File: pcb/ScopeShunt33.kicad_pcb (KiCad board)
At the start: 2 copper layers, 50 x 50 mm, 35 parts, among them J1 Screw_Terminal_01x02, J2 Conn_Coaxial

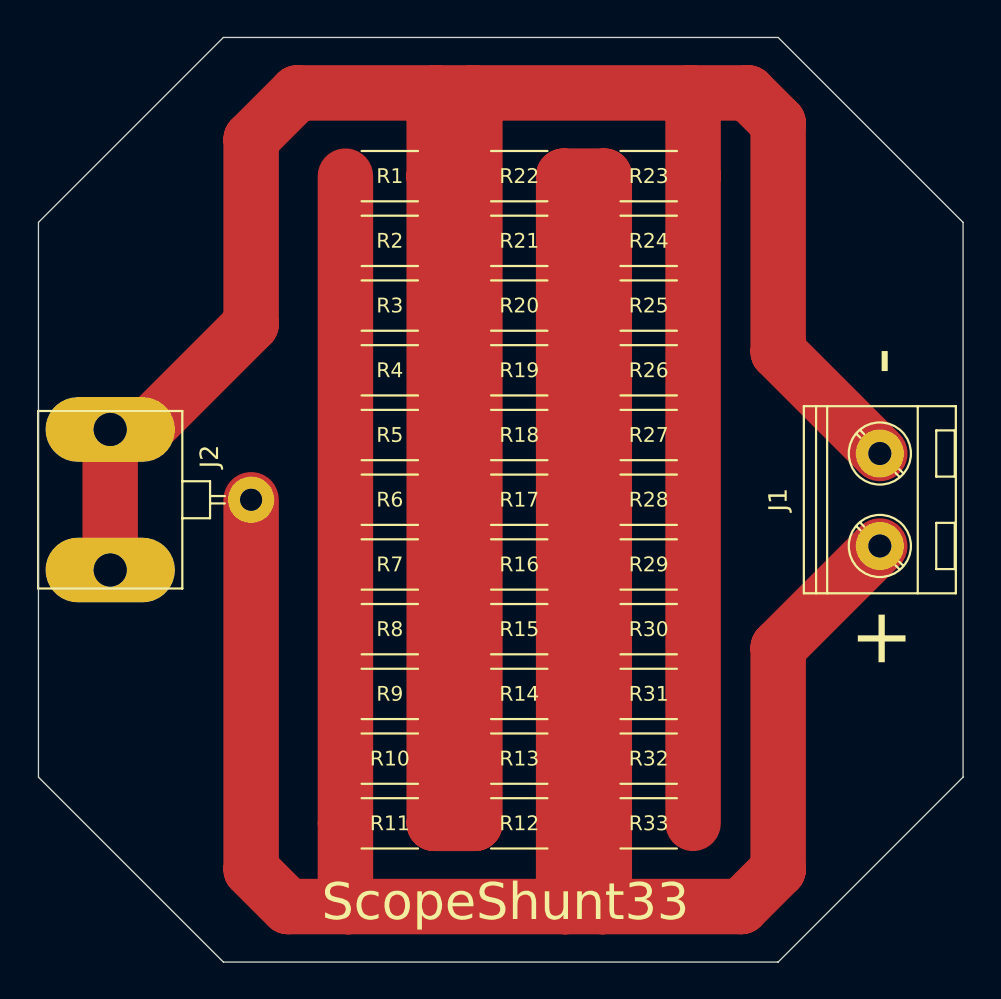
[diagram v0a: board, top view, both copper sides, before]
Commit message: smaller pcb
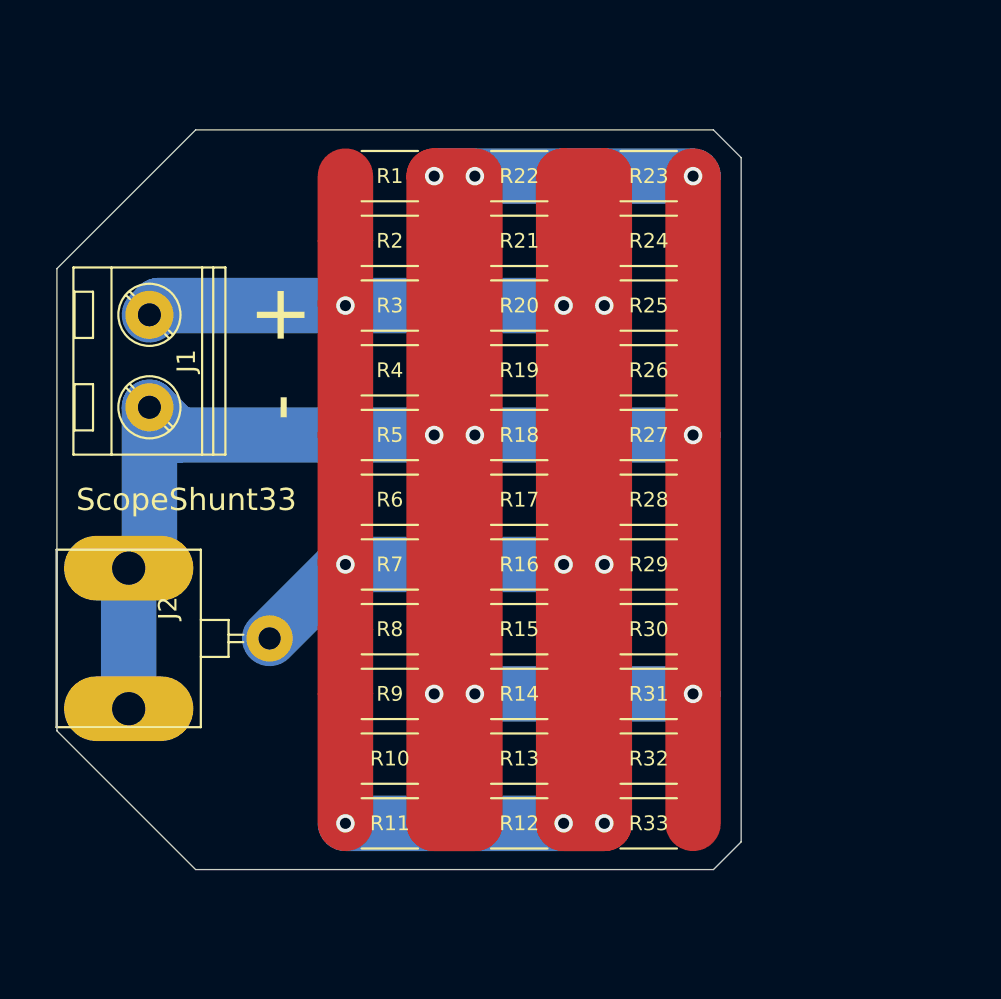
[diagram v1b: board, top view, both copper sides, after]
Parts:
- moved J1 39.6 mm to (131.0, 95.0), turned to 90 degrees
- moved J2 7.57 mm to (137.5, 107.5)
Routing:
- net /+: track 193.0 -> 168.0 mm, vias 0 -> 9
- net /-: track 201.0 -> 184.0 mm, vias 0 -> 9
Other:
- board size 50 x 50 mm -> 37 x 40 mm
- board text added: "Connect + & - in series with load"
- board text added: "LOAD"
- board text added: "SCOPE"
- board text added: "for measuring current with oscilloscope"
- board text added: "github.com/bkw777/ScopeShunt33 - v003"
- board text added: "shunt resistor"
- board text removed: "Connect + & - in series with load."
- board text removed: "Inspired by github.com/voltlog/ScopeShunt"
- board text removed: "Shunt resistor for measuring current with oscilloscope."
- board text removed: "github.com/bkw777/ScopeShunt33"
- board text removed: "v002"

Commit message: connector arrangement
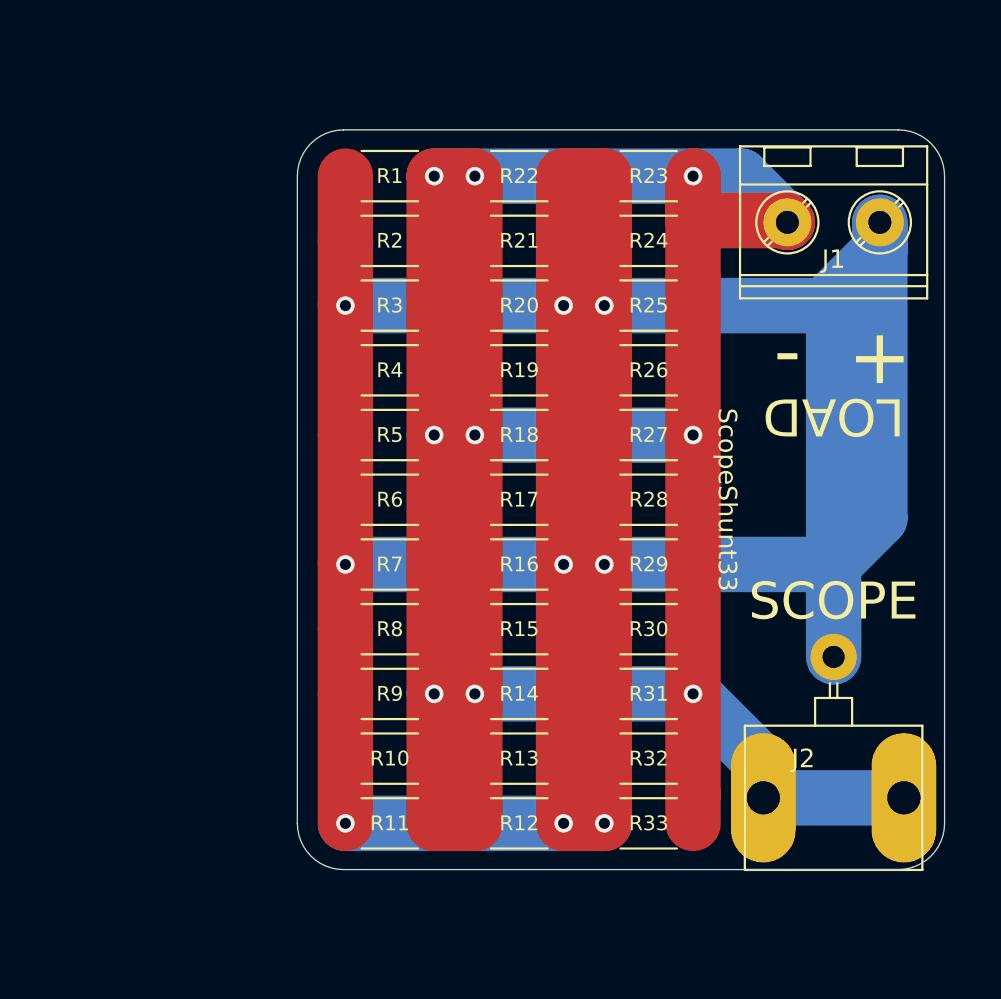
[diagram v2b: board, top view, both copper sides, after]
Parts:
- moved J1 35.9 mm to (165.5, 85.0), turned to 0 degrees
- moved J2 30.5 mm to (168.0, 108.5), turned to 180 degrees
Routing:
- net /+: track 168.0 -> 220.2 mm
- net /-: track 184.0 -> 179.7 mm
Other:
- board size 37 x 40 mm -> 35 x 40 mm
- board text added: "connect + & - in series with load"
- board text added: "github.com/bkw777/ScopeShunt33 - v004"
- board text removed: "Connect + & - in series with load"
- board text removed: "github.com/bkw777/ScopeShunt33 - v003"

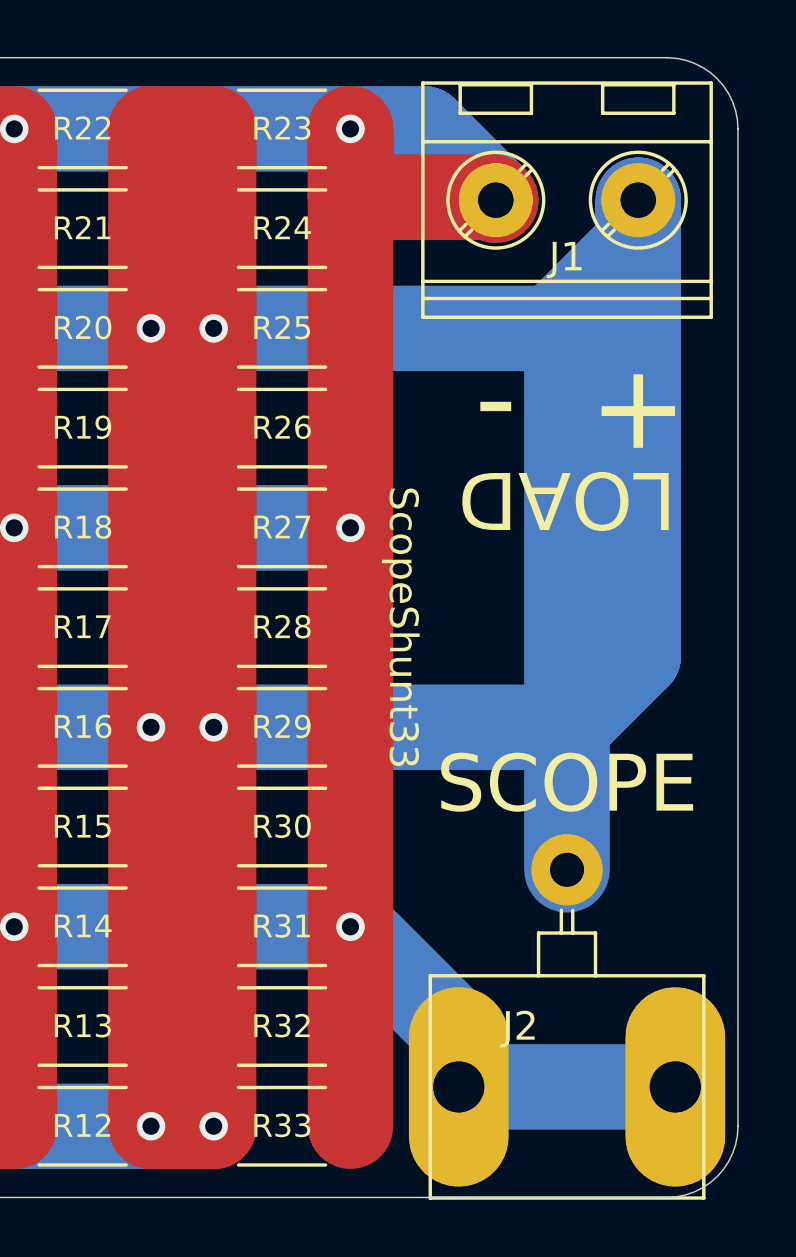
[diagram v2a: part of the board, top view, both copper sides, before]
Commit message: enclosure printability & part fitment
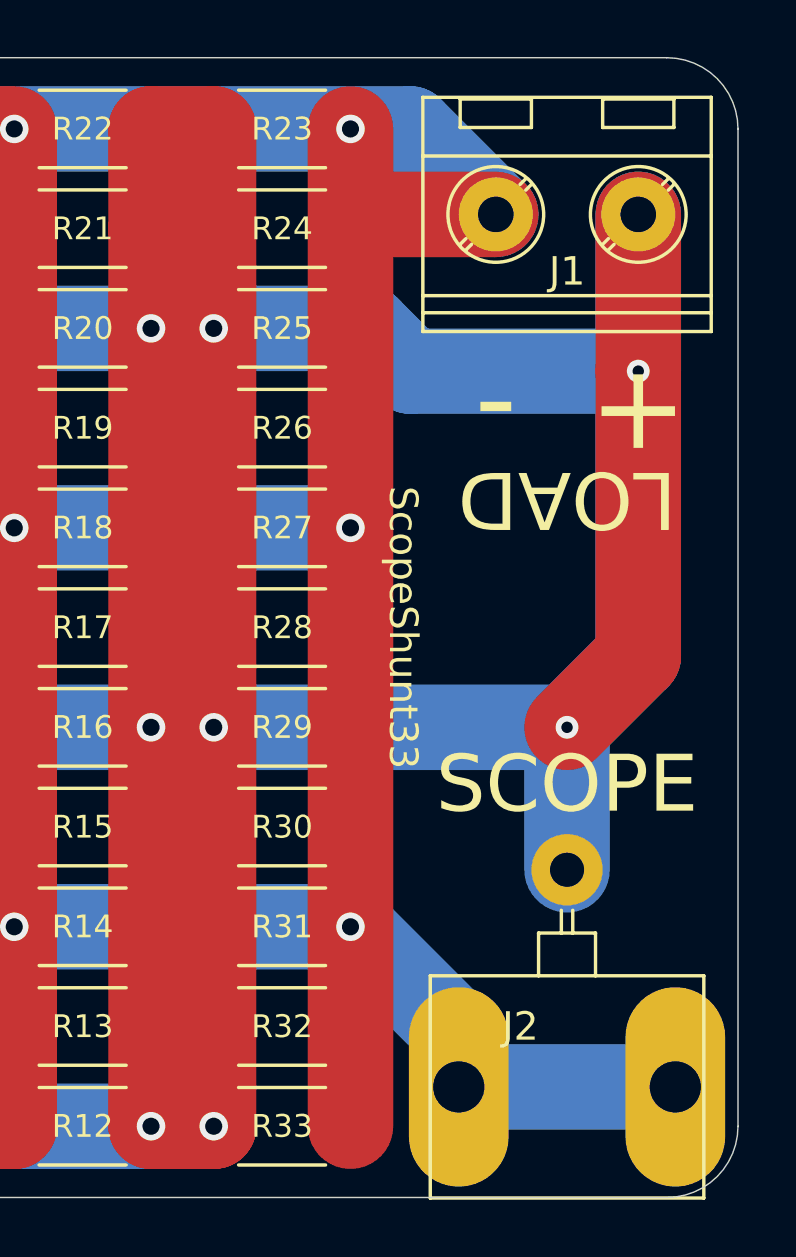
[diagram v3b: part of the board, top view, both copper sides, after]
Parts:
- moved J1 0.50 mm to (165.5, 85.5)
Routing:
- net /+: track 220.2 -> 227.9 mm, vias 9 -> 11
- net /-: track 179.7 -> 177.7 mm
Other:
- board text added: "github.com/bkw777/ScopeShunt33 - v005"
- board text removed: "github.com/bkw777/ScopeShunt33 - v004"

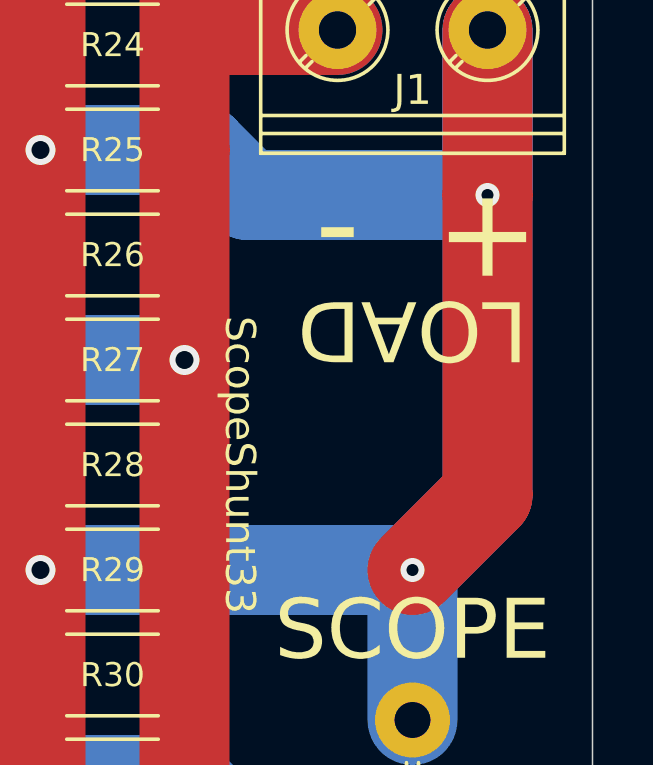
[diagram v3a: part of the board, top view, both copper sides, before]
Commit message: via sizes
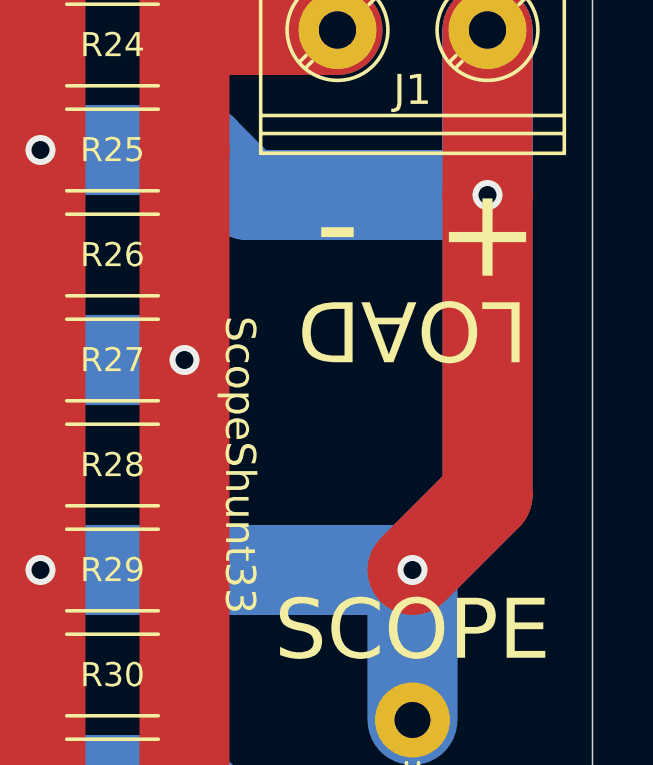
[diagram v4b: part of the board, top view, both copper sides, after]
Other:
- board text added: "github.com/bkw777/ScopeShunt33 - v006"
- board text removed: "github.com/bkw777/ScopeShunt33 - v005"
